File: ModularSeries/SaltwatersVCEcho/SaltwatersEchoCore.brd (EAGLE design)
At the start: 74.8 x 100 mm, 111 parts, among them IC1 PT2399DIL16, Q1 2N3906, Q2 2N3906, Q3 2N3906, Q4 2N3906, Q5 2N3904, Q6 2N3904

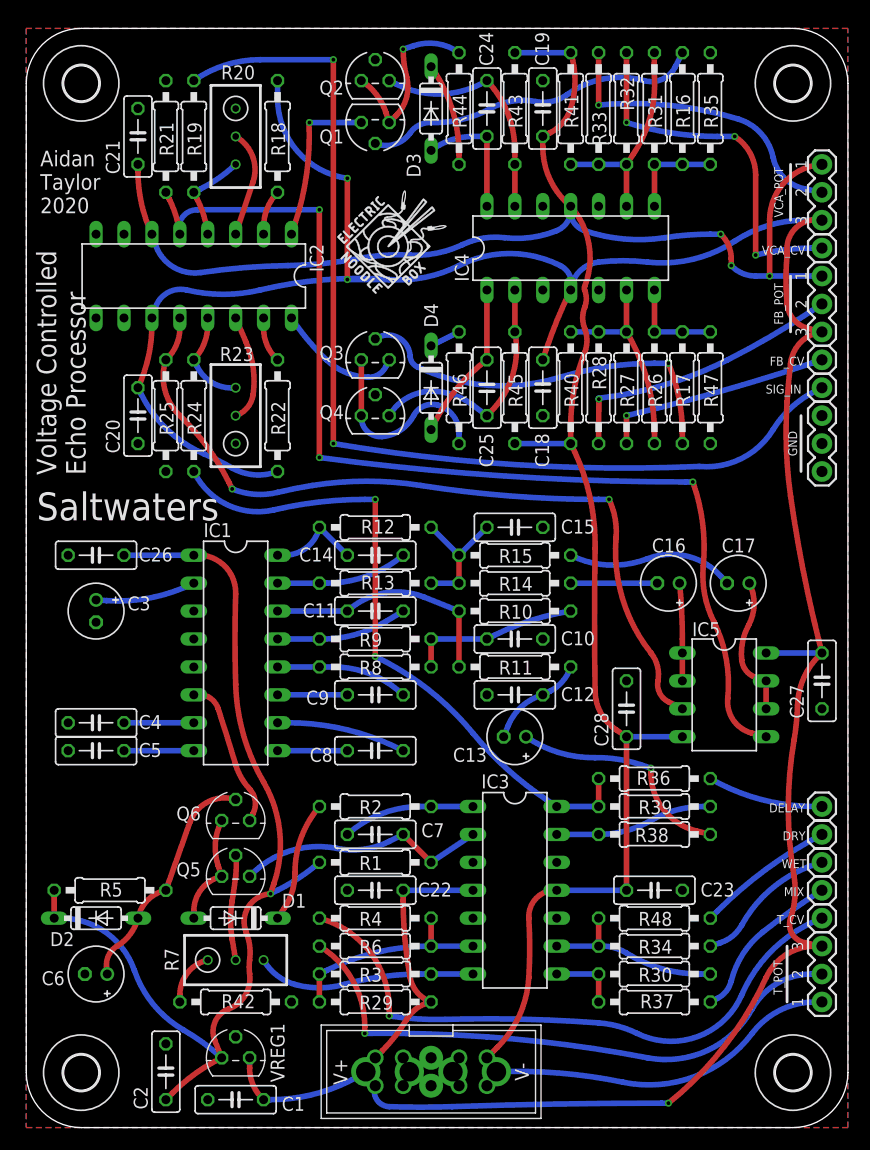
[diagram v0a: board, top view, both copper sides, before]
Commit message: All active BOMs updated to new header standard
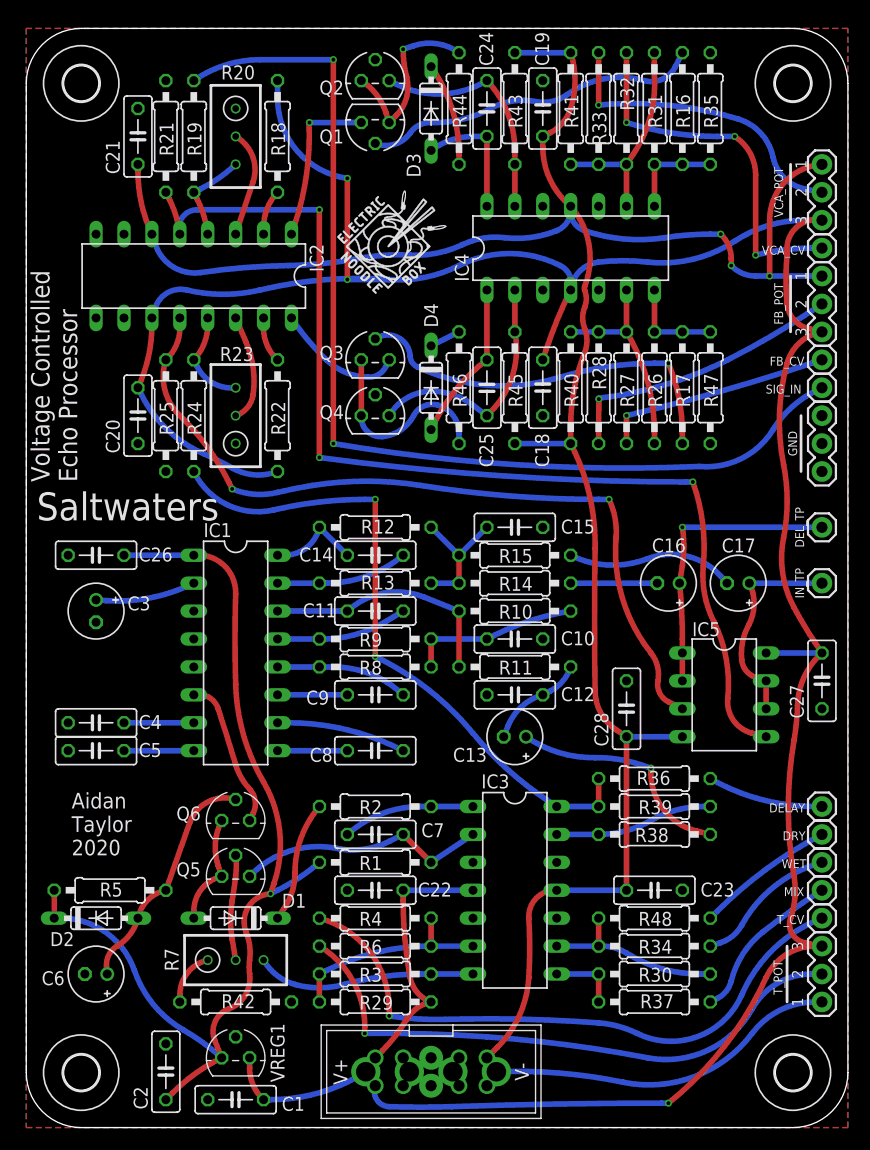
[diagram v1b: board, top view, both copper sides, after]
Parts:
- added DEL_TP, IN_TP: 1XWIREPAD, ElectricNoodleBox:1X01
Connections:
- net FB_RTN: now also DEL_TP.1
- net N$34: now also IN_TP.1
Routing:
- net FB_RTN: track 8.90 -> 26.7 mm, vias 0 -> 1
- net N$34: track 12.6 -> 19.2 mm
- net +12V: track 285.7 -> 286.4 mm
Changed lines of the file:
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@@
 <setting verticaltext="up"/>
 </settings>
-<grid distance="1.27" unitdist="mm" unit="mm" style="lines" multiple="1" display="no" altdistance="5" altunitdist="mil" altunit="mil"/>
+<grid distance="12.5" unitdist="mil" unit="mil" style="lines" multiple="1" display="no" altdistance="5" altunitdist="mil" altunit="mil"/>
 <layers>
 <layer number="1" name="Top" color="4" fill="1" visible="yes" active="yes"/>
@@
 </layers>
 <board>
+<fusionsync huburn="a.cGVyc29uYWw6dWUyYjdlNGE0" projecturn="a.cGVyc29uYWw6dWUyYjdlNGE0IzIwMjAwNDA1MjgzMzA0MTgx" f3durn="urn:adsk.wipprod:dm.lineage:ALBxLM8FSLGiyH-Wd44oqg" pcbguid="" lastpulledtime="" lastsyncedchangeguid="" latestrevisionid="546f434c-34c4-432b-946a-7654f913916c" lastsyncedrevisionid="546f434c-34c4-432b-946a-7654f913916c" lastboardhashguid="53e9d930-aeab-c7a9-fca4-e91a252a806a" lastpushedtime="2021-01-03T09:50:09Z" linktopcb3d="true"/>
 <plain>
 <wire x1="70.485" y1="64.77" x2="70.485" y2="59.69" width="0.254" layer="21"/>
@@
 <text x="70.1675" y="16.51" size="1.016" layer="21" font="vector" ratio="12" rot="R90" align="center">3</text>
 <wire x1="69.215" y1="16.51" x2="69.215" y2="11.43" width="0.254" layer="21"/>
-<text x="1.27" y="83.185" size="1.4224" layer="21" font="vector" ratio="16">Aidan
+<text x="4.1275" y="24.765" size="1.4224" layer="21" font="vector" ratio="16">Aidan
 Taylor
 2020</text>
 <text x="0.9525" y="56.515" size="2.54" layer="21" font="vector" ratio="16" rot="R180" align="center-right">Saltwaters</text>
-<text x="3.175" y="59.3725" size="1.778" layer="21" font="vector" ratio="16" rot="R90" align="center-left">Voltage Controlled
+<text x="2.54" y="58.7375" size="1.6764" layer="21" font="vector" ratio="16" rot="R90" align="center-left">Voltage Controlled
 Echo Processor</text>
 <wire x1="0" y1="95" x2="0" y2="5" width="0" layer="20"/>
@@
 <element name="U$1" library="ElectricNoodleBox" package="LOGO10X10" value="" x="28.2575" y="75.565" smashed="yes"/>
 <element name="U$2" library="ElectricNoodleBox" package="LOGO10X10" value="" x="38.4175" y="75.565" smashed="yes" rot="MR0"/>
+<element name="IN_TP" library="ElectricNoodleBox" package="1X01" value="1XWIREPAD" x="72.39" y="49.53" smashed="yes">
+<attribute name="NAME" x="70.358" y="49.53" size="0.8128" layer="25" font="vector" ratio="20" rot="R90" align="center"/>
+<attribute name="VALUE" x="71.12" y="48.006" size="0.8128" layer="27" font="vector" ratio="20" align="top-left"/>
+</element>
+<element name="DEL_TP" library="ElectricNoodleBox" package="1X01" value="1XWIREPAD" x="72.39" y="54.61" smashed="yes">
+<attribute name="NAME" x="70.358" y="54.61" size="0.8128" layer="25" font="vector" ratio="20" rot="R90" align="center"/>
+<attribute name="VALUE" x="71.12" y="53.086" size="0.8128" layer="27" font="vector" ratio="20" align="top-left"/>
+</element>
 </elements>
 <signals>
@@
 <wire x1="69.85" y1="35.2425" x2="70.1675" y2="38.4175" width="0.508" layer="1" curve="7.924825"/>
 <wire x1="70.1675" y1="38.4175" x2="72.39" y2="43.18" width="0.508" layer="1" curve="-46.537406"/>
-<wire x1="72.39" y1="43.18" x2="72.0725" y2="44.45" width="0.508" layer="1"/>
-<wire x1="72.0725" y1="44.45" x2="69.5325" y2="57.4675" width="0.508" layer="1" curve="-5.990607"/>
-<wire x1="69.5325" y1="57.4675" x2="69.215" y2="66.04" width="0.508" layer="1" curve="-11.8491"/>
-<wire x1="69.215" y1="66.04" x2="69.5325" y2="69.5325" width="0.508" layer="1" curve="-2.781952"/>
-<wire x1="69.5325" y1="69.5325" x2="72.39" y2="72.39" width="0.508" layer="1" curve="-76.829198"/>
 <wire x1="72.39" y1="72.39" x2="71.12" y2="72.7075" width="0.508" layer="1"/>
 <wire x1="71.12" y1="72.7075" x2="69.215" y2="74.93" width="0.508" layer="1" curve="-70.724902"/>
@@
 <wire x1="29.21" y1="77.1525" x2="33.02" y2="77.1525" width="0.508" layer="16"/>
 <wire x1="29.21" y1="86.36" x2="29.21" y2="77.1525" width="0.508" layer="1"/>
+<wire x1="72.39" y1="43.18" x2="71.755" y2="44.1325" width="0.508" layer="1"/>
+<wire x1="71.755" y1="44.1325" x2="69.85" y2="47.3075" width="0.508" layer="1" curve="-5.452622"/>
+<wire x1="69.85" y1="47.3075" x2="68.8975" y2="53.6575" width="0.508" layer="1" curve="-39.413422"/>
+<wire x1="68.8975" y1="53.6575" x2="68.8975" y2="60.325" width="0.508" layer="1" curve="22.351828"/>
+<wire x1="68.8975" y1="60.325" x2="69.215" y2="69.5325" width="0.508" layer="1" curve="-26.301696"/>
+<wire x1="69.215" y1="69.5325" x2="72.39" y2="72.39" width="0.508" layer="1" curve="-65.77402"/>
 </signal>
 <signal name="+5V">
@@
 <wire x1="59.69" y1="43.18" x2="59.69" y2="44.45" width="0.508" layer="1"/>
 <wire x1="59.69" y1="44.45" x2="59.436" y2="49.53" width="0.508" layer="1" curve="5.72481"/>
+<contactref element="DEL_TP" pad="1"/>
+<wire x1="59.436" y1="49.53" x2="59.69" y2="51.1175" width="0.508" layer="1"/>
+<wire x1="59.69" y1="51.1175" x2="59.69" y2="54.61" width="0.508" layer="1" curve="18.180554"/>
+<via x="59.69" y="54.61" extent="1-16" drill="0.35"/>
+<wire x1="59.69" y1="54.61" x2="72.39" y2="54.61" width="0.508" layer="16"/>
 </signal>
 <signal name="N$32">
@@
 <wire x1="65.0875" y1="42.545" x2="65.7225" y2="45.72" width="0.508" layer="1" curve="-34.128954"/>
 <wire x1="65.7225" y1="45.72" x2="65.786" y2="49.53" width="0.508" layer="1" curve="54.839105"/>
+<contactref element="IN_TP" pad="1"/>
+<wire x1="65.786" y1="49.53" x2="72.39" y2="49.53" width="0.508" layer="16"/>
 </signal>
 <signal name="INPUT">
@@
 </note>
 <note version="8.3" severity="warning">
+Since Version 8.3, EAGLE supports Fusion synchronisation.
+This feature will not be available in this version and saving
+the document will break the link to the Fusion PCB feature.
+</note>
+<note version="8.3" severity="warning">

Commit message: Saltwaters BOM added
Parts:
- C10: value 5.6nF -> 4.7nF
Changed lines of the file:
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@@
 <attribute name="VALUE" x="22.479" y="5.334" size="1.27" layer="27" ratio="10" rot="R180"/>
 </element>
-<element name="C10" library="rcl" library_urn="urn:adsk.eagle:library:334" package="C050-025X075" package3d_urn="urn:adsk.eagle:package:23637/1" value="5.6nF" x="44.45" y="44.45" smashed="yes" rot="R180">
+<element name="C10" library="rcl" library_urn="urn:adsk.eagle:library:334" package="C050-025X075" package3d_urn="urn:adsk.eagle:package:23637/1" value="4.7nF" x="44.45" y="44.45" smashed="yes" rot="R180">
 <attribute name="NAME" x="48.641" y="43.8785" size="1.27" layer="25" ratio="10"/>
 <attribute name="POPULARITY" value="29" x="27.94" y="80.01" size="1.778" layer="27" rot="R180" display="off"/>

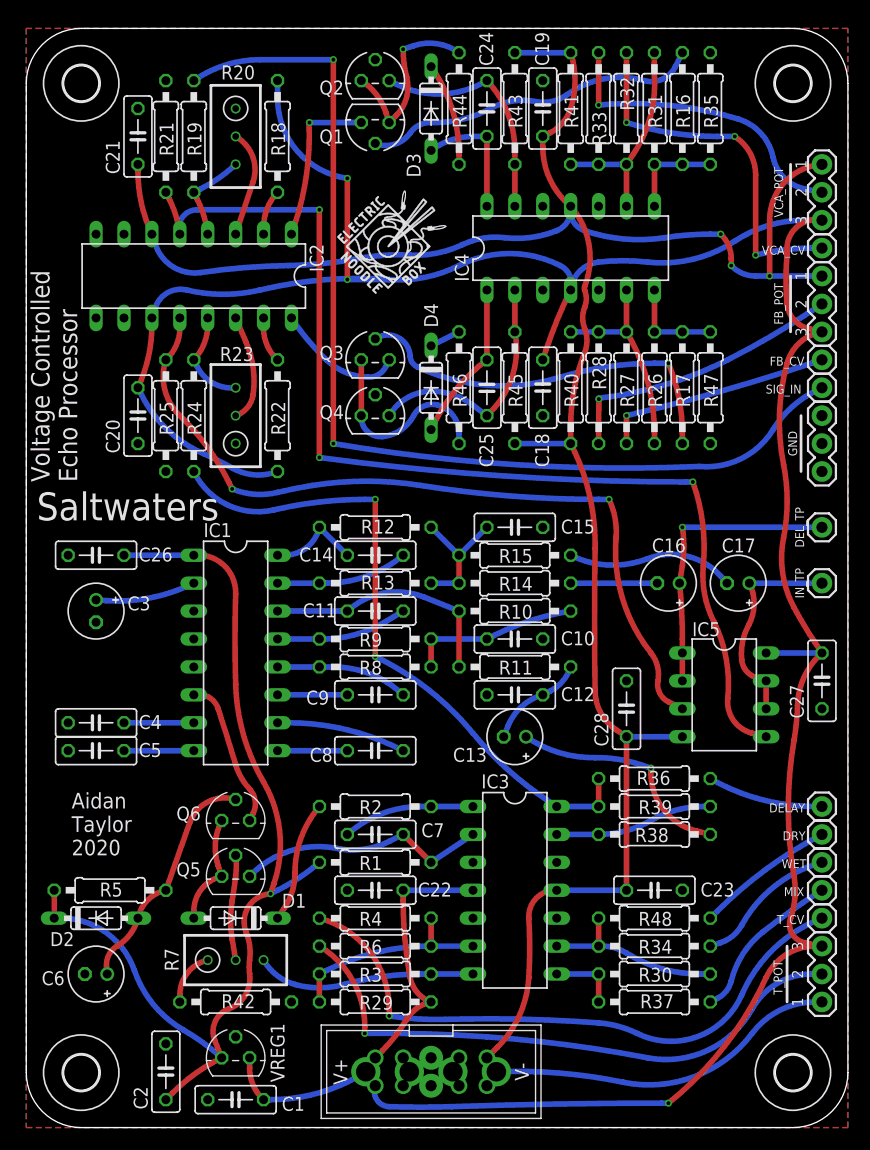
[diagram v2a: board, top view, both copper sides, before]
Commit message: Saltwaters core schematics corrections update
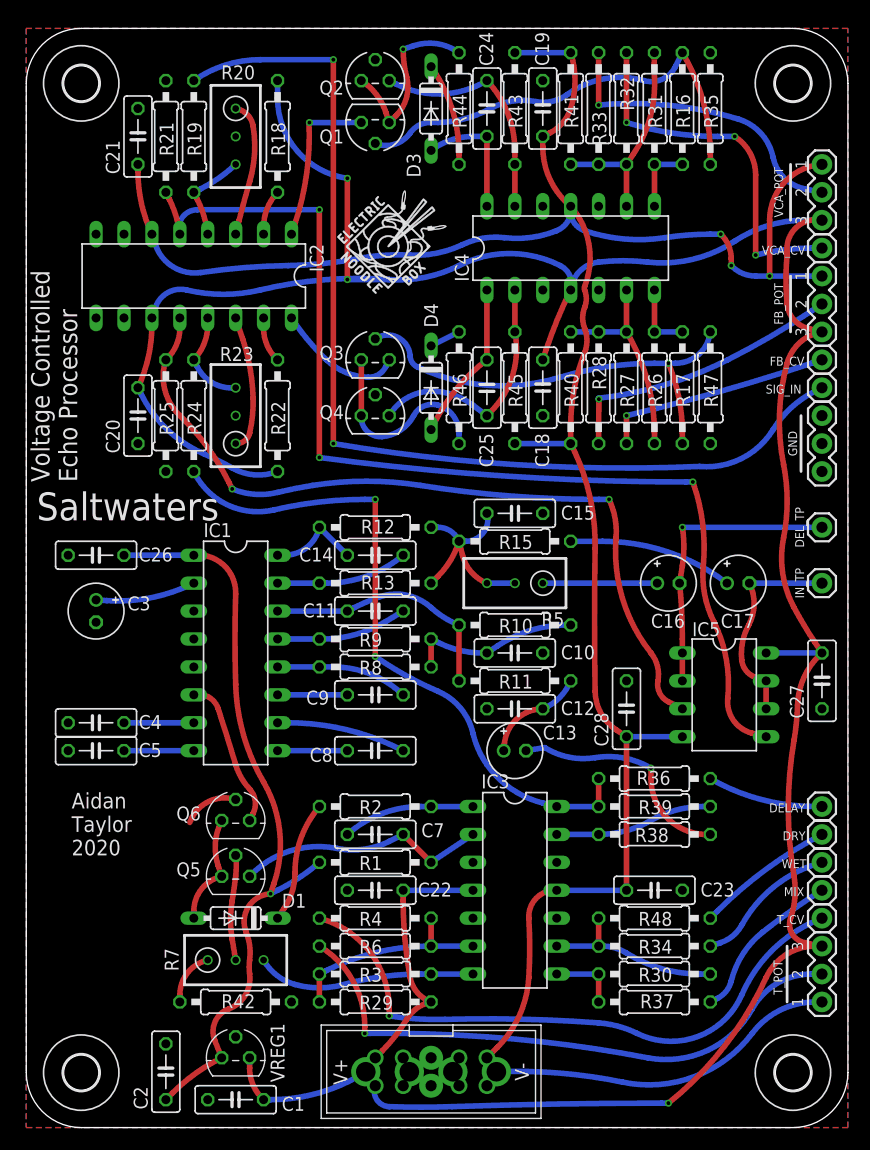
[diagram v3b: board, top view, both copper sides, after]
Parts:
- removed C6: 1µF, rcl:E2-5
- removed D2: BAT85, ElectricNoodleBox:DO35-7
- removed R14: 15K, rcl:0207/10
- C10: value 4.7nF -> 10nF
- C12: value 10nF -> 470nF
- R1: value 47K -> 10K
- R11: value 7K5 -> 100Ω
- R16, R17: value 1K -> 75Ω
- R18, R22: value 5K7 -> 5K6
- R30, R34, R48: value 100Ω -> 100K
- R35, R47: value 10K -> 75Ω
- R43, R45: value 120K -> 100K
- R5: value 100K -> 47K; device rcl:0207/10 -> rcl:RTRIM3296W
- moved R5 46.2 mm to (44.5, 49.5), turned to 90 degrees
- moved C10 1.27 mm to (44.5, 43.2)
- moved C13 1.27 mm to (44.5, 34.3), turned to 0 degrees
- moved C15 1.27 mm to (44.5, 55.9)
- moved R10 1.27 mm to (44.5, 45.7)
- moved R15 1.27 mm to (44.5, 53.3)
- moved C12 1.27 mm to (44.5, 38.1)
- moved R11 1.27 mm to (44.5, 40.6)
- turned C16 to 0 degrees
- turned C17 to 0 degrees
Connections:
- removed net N$8: C6.+, D2.A, Q6.2, R5.1
- net +5V: no longer D2.C, R5.2
- net AGND: now also Q6.2, R20.2, R23.2; no longer C6.-, R20.1, R23.1
- net FB_RTN: now also C16.-; no longer C16.+
- net N$22: now also R35.2
- net N$23: now also C13.+; no longer C13.-
- net N$26: now also R5.2, R5.3; no longer R14.2
- net N$27: now also C17.+, R15.1; no longer C16.-, R14.1
- net N$28: now also C16.+, R5.1; no longer C17.-, R15.1
- net N$30: now also R20.1; no longer R20.2
- net N$31: no longer R47.2
- net N$34: now also C17.-; no longer C17.+
- net N$38: now also R23.1; no longer R23.2
- net N$41: now also R47.2
- net N$44: no longer R35.2
- net N$51: now also C13.-; no longer C13.+
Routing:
- net +5V: track 90.1 -> 67.4 mm
- net N$8: track 20.7 -> 0.00 mm
- net N$22: track 29.7 -> 40.2 mm
- net N$27: track 7.87 -> 14.8 mm
- net N$26: track 12.3 -> 18.6 mm
- net N$41: track 35.1 -> 40.0 mm
- net AGND: track 0.00 -> 4.67 mm
- net N$28: track 14.7 -> 10.4 mm
- net N$30: track 9.44 -> 12.3 mm
- net N$38: track 9.70 -> 12.3 mm
- net N$44: track 8.89 -> 6.35 mm
- net N$31: track 8.89 -> 6.35 mm
- net DELAY_SIG: track 59.4 -> 60.1 mm
